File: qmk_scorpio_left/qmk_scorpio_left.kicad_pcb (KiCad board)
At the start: 2 copper layers, 174.2 x 117.5 mm, 149 parts, among them J1 USB_C_Receptacle_USB2.0, J2 Conn_01x05, J3 USB_C_Receptacle_USB2.0, Q3 MMUN2133LT1G, U1 STM32G474CETx, U2 PRTR5V0U2X, U3 XC6206PxxxMR-Regulator_Linear, U4 CR2013-MI2120, U5 PRTR5V0U2X

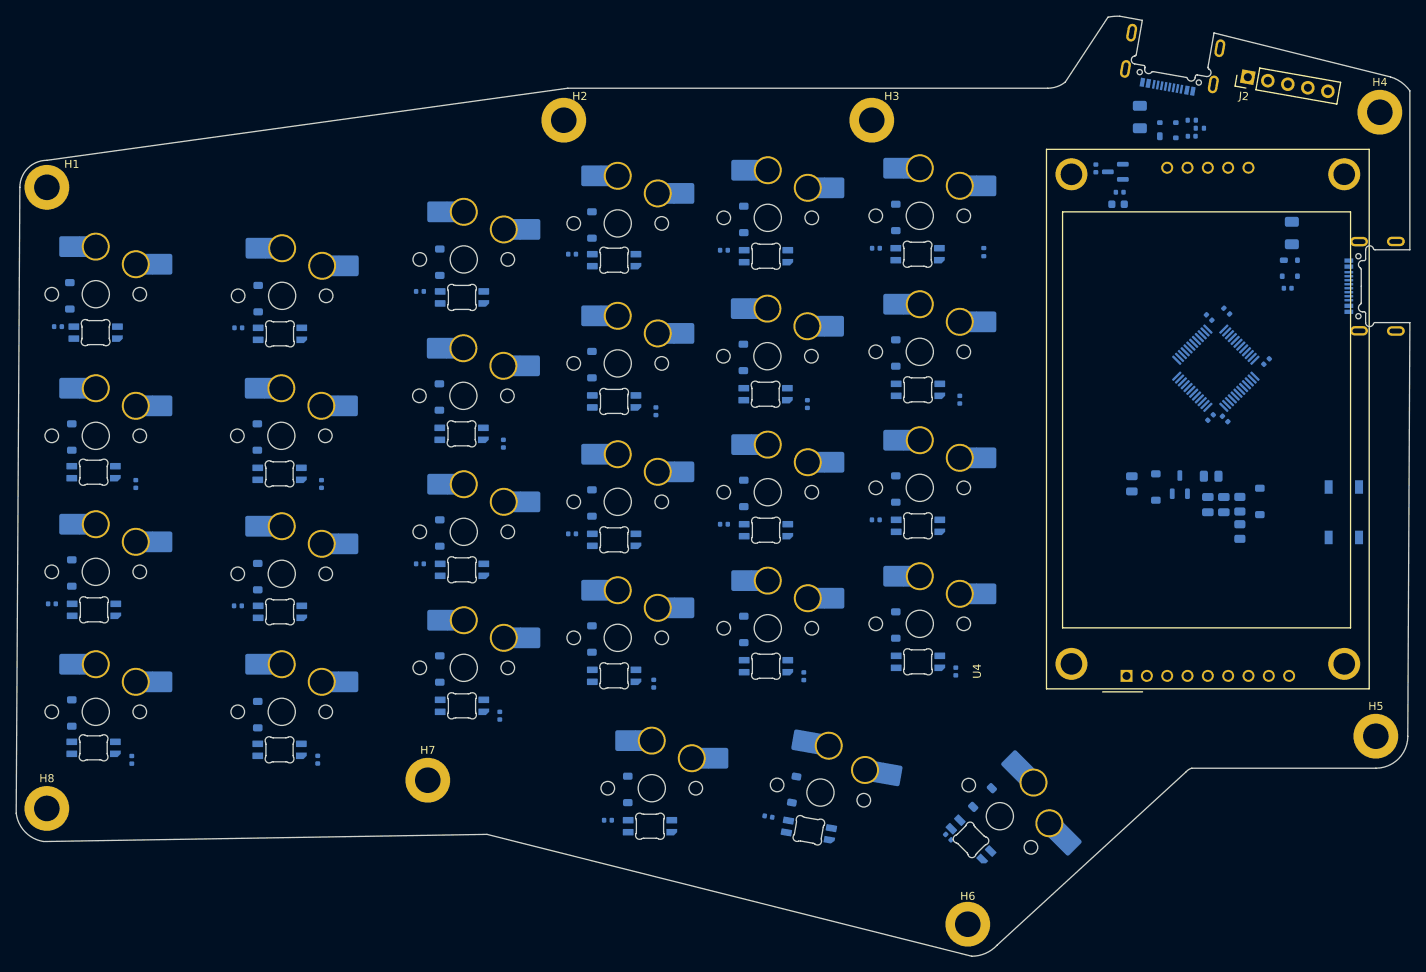
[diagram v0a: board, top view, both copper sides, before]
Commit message: fixed col/row connections in matrix schematics
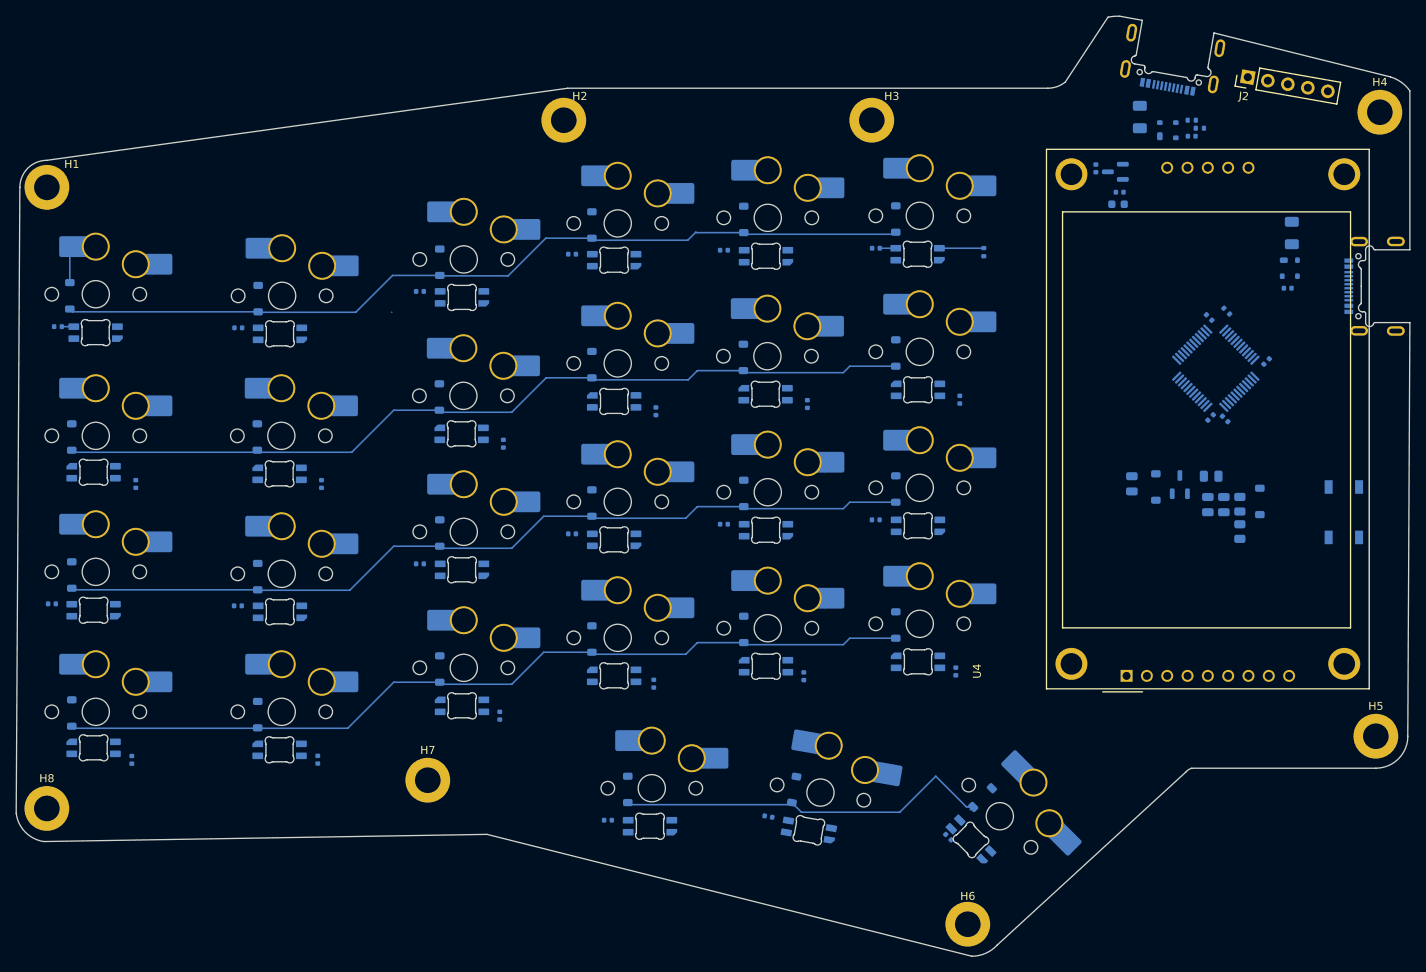
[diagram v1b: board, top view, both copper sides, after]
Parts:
- moved D13 0.25 mm to (82.0, 104.8)
- moved D6 0.20 mm to (185.0, 60.4)
- moved LED13 0.07 mm to (84.7, 109.2)
- turned LED10 to 180 degrees
- turned LED11 to 180 degrees
- turned LED12 to 180 degrees
- turned LED19 to 180 degrees
- turned LED20 to 180 degrees
- turned LED21 to 180 degrees
- turned LED22 to 180 degrees
- turned LED23 to 180 degrees
- turned LED24 to 180 degrees
- turned LED7 to 180 degrees
- turned LED8 to 180 degrees
- turned LED9 to 180 degrees
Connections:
- CH12 pad 1: col0 -> col5
- CH14 pad 1: col0 -> col1
- CH15 pad 1: col0 -> col2
- CH18 pad 1: col0 -> col5
- CH2 pad 1: col0 -> col1
- CH20 pad 1: col0 -> col1
- CH21 pad 1: col0 -> col2
- CH24 pad 1: col0 -> col5
- CH27 pad 1: col0 -> col5
- CH3 pad 1: col0 -> col2
- CH6 pad 1: col0 -> col5
- CH8 pad 1: col0 -> col1
- CH9 pad 1: col0 -> col2
- D19 pad 1: col0 -> row3
- D20 pad 1: col0 -> row3
- D21 pad 1: col0 -> row3
- D22 pad 1: col0 -> row3
- D23 pad 1: col0 -> row3
- D24 pad 1: col0 -> row3
- U1 pad 17: col0 -> col5
- U1 pad 27: col0 -> row3
- U1 pad 28: col0 -> col2
- U1 pad 3: col0 -> col1
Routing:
- net row1: track 0.00 -> 108.8 mm
- net row3: track 0.00 -> 108.4 mm
- net row2: track 0.00 -> 108.4 mm
- net row0: track 0.00 -> 108.0 mm
- net row4: track 0.00 -> 47.9 mm
- net RGB5v: track 0.00 -> 5.56 mm
- net Net-(D1-A): track 0.00 -> 4.50 mm
- net +5V: track 0.00 -> 3.50 mm

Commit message: keys routed
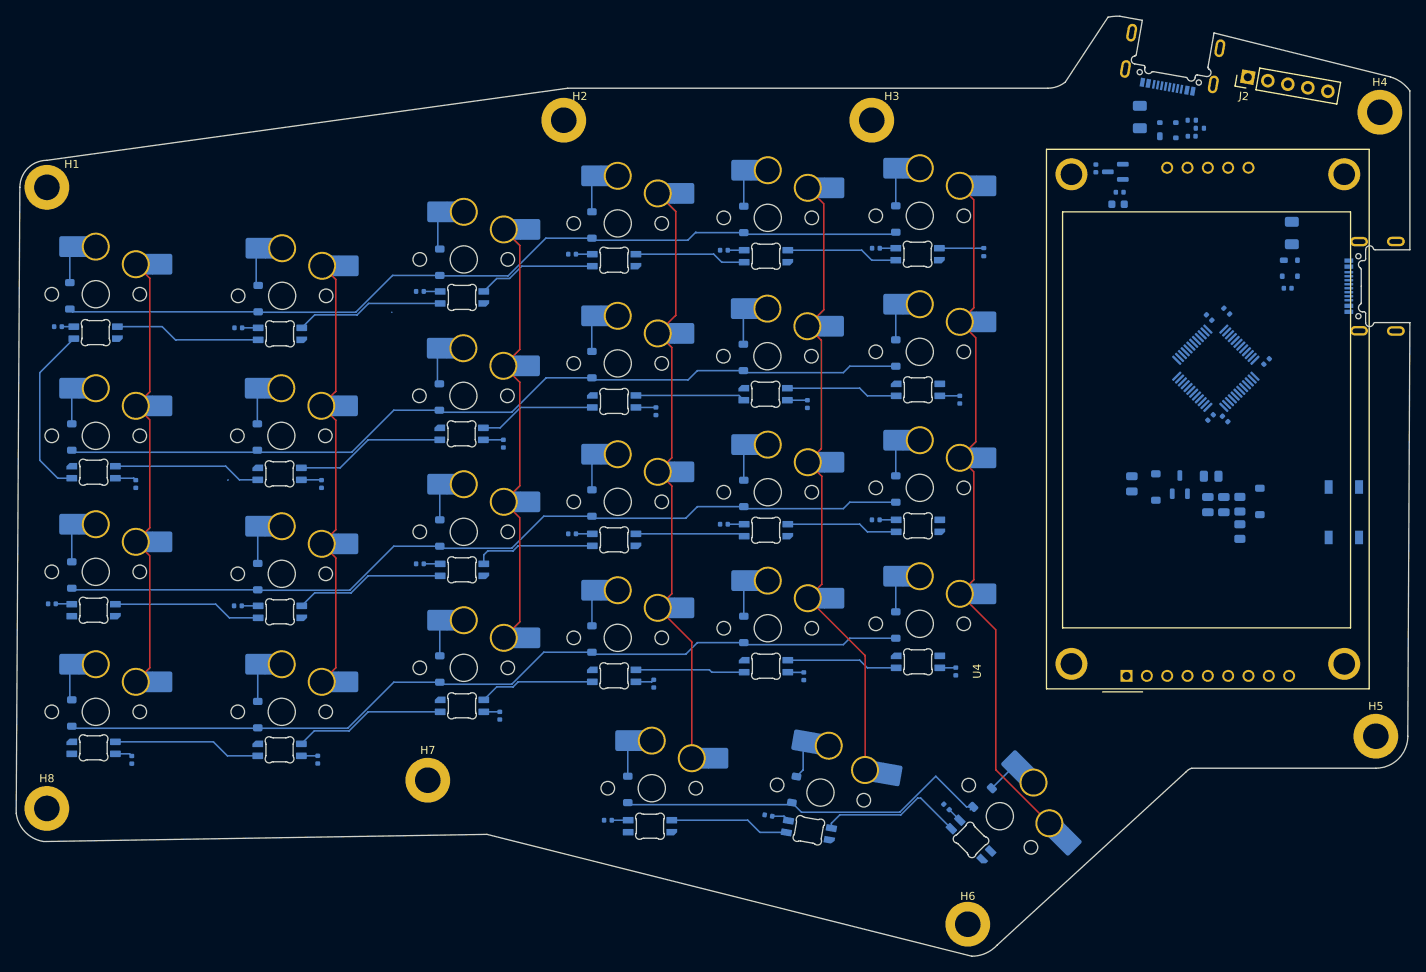
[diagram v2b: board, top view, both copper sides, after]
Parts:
- moved C27 3.78 mm to (191.3, 133.8)
- moved C26 0.13 mm to (169.1, 134.9)
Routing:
- net col5: track 0.00 -> 88.9 mm
- net col4: track 0.00 -> 80.3 mm
- net col3: track 0.00 -> 77.1 mm
- net col0: track 0.00 -> 56.5 mm
- net col1: track 0.00 -> 56.4 mm
- net col2: track 0.00 -> 56.1 mm
- net +5V: track 3.50 -> 57.9 mm
- net DOut1: track 0.00 -> 21.9 mm
- net Net-(LED20-DOUT): track 0.00 -> 19.0 mm
- net Net-(LED14-DIN): track 0.00 -> 18.9 mm
- net Net-(LED8-DOUT): track 0.00 -> 18.8 mm
- net Net-(LED7-DOUT): track 0.00 -> 18.6 mm
- net Net-(LED2-DIN): track 0.00 -> 18.6 mm
- net Net-(LED13-DIN): track 0.00 -> 18.5 mm
- net Net-(LED19-DOUT): track 0.00 -> 18.5 mm
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
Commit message: placed 5V vias
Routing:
- net DOut4: track 0.00 -> 34.4 mm, vias 0 -> 2
- net +5V: track 57.9 -> 87.3 mm, vias 0 -> 28
- net DOut2: track 0.00 -> 26.6 mm
- net DOut3: track 0.00 -> 21.0 mm
- net VBUS: track 0.00 -> 3.39 mm
- net row4: track 47.9 -> 50.7 mm
- net Net-(LED22-DOUT): track 14.1 -> 16.1 mm
- net Net-(LED23-DOUT): track 13.9 -> 15.9 mm
- net Net-(LED11-DOUT): track 14.0 -> 16.0 mm
- net Net-(LED7-DOUT): track 18.6 -> 20.2 mm
- net RGB5v: track 5.56 -> 7.04 mm, vias 0 -> 1
